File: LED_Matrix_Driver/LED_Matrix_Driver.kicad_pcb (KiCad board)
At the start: 4 copper layers, 200.7 x 66 mm, 73 parts, among them J1 Screw_Terminal_01x02, J2 LED Anode Rows, J3 Columns 24-31 LED Cathodes, J4 Columns 16-23 LED Cathodes, J5 Columns 8-15 LED Cathodes, J6 Columns 0-7 LED Cathodes, J7 Buttons, U1 ESP32-DEVKITC-32E, U2 74HCT244, U3 MIC2981, U4 74HC238, U5 HEF4794B, U6 HEF4794B, U7 HEF4794B, U8 HEF4794B

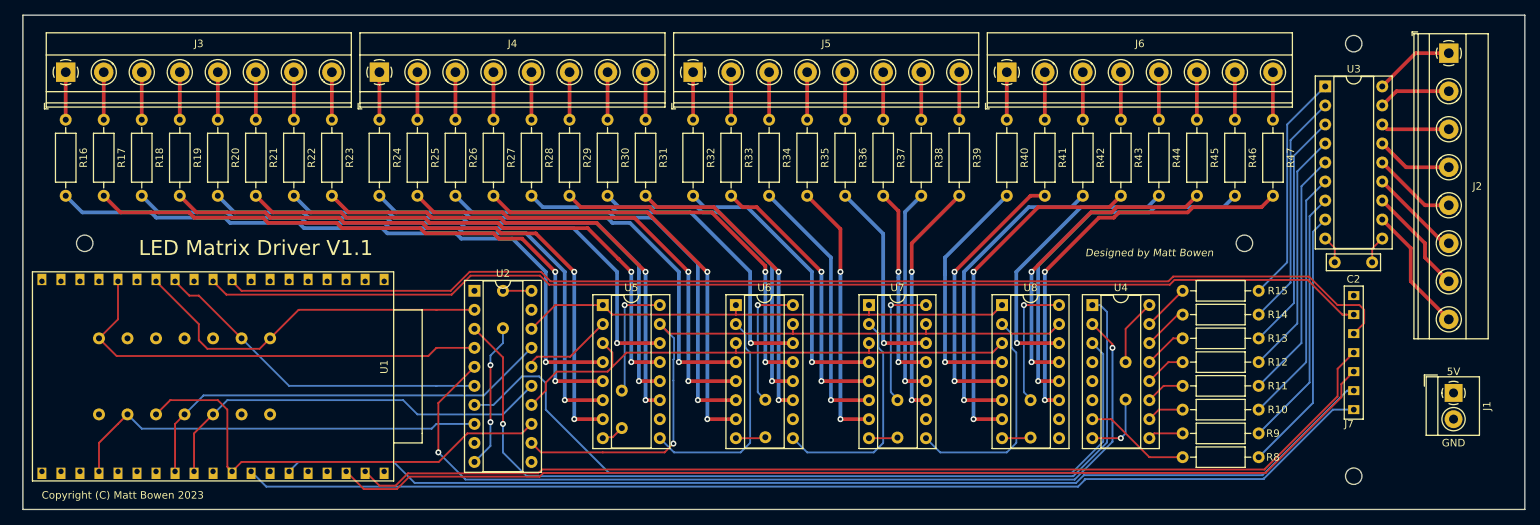
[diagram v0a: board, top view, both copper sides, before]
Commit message: Added audio input circuitry for potential audio applications
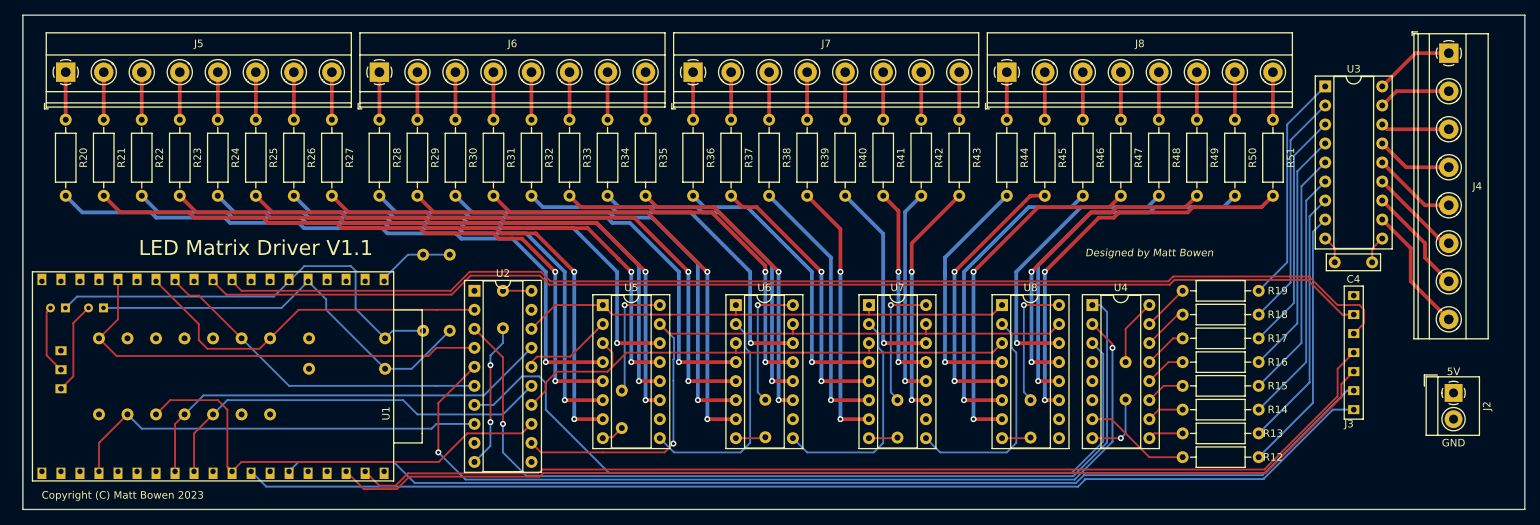
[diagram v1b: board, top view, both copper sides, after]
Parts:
- removed  : , MountingHole:MountingHole_2.2mm_M2 (x4)
- added C1: 1uF, Capacitor_THT:CP_Radial_D4.0mm_P2.00mm, B.Cu at (20.3, 49.3)
- added C2: 1uF, Capacitor_THT:CP_Radial_D4.0mm_P2.00mm, B.Cu at (15.2, 49.3)
- added J1: Audio In, Arduino:Custom_Pin_Header_3, B.Cu at (15.2, 62.0)
- added R1: 10k, Resistor_THT:R_Axial_DIN0207_L6.3mm_D2.5mm_P10.16mm_Horizontal, B.Cu at (66.5, 52.3)
- added R2: 10k, Resistor_THT:R_Axial_DIN0207_L6.3mm_D2.5mm_P10.16mm_Horizontal, B.Cu at (47.8, 57.4)
- added R3: 10k, Resistor_THT:R_Axial_DIN0207_L6.3mm_D2.5mm_P10.16mm_Horizontal, B.Cu at (63.0, 52.3)
- added R4: 10k, Resistor_THT:R_Axial_DIN0207_L6.3mm_D2.5mm_P10.16mm_Horizontal, B.Cu at (47.8, 53.3)
- J3: renamed from J7; footprint Arduino:Custom_Pin_Header -> Arduino:Custom_Pin_Header_7
- renumbered C1 to C3, C2 to C4, C3 to C5, C4 to C6, C5 to C7, C6 to C8, C7 to C9, J1 to J2, J2 to J4, J3 to J5, J4 to J6, J5 to J7, J6 to J8, R6 to R10, R7 to R11, R8 to R12, R9 to R13, R10 to R14, R11 to R15, R12 to R16, R13 to R17, R14 to R18, R15 to R19, R16 to R20, R17 to R21, R18 to R22, R19 to R23, R20 to R24, R21 to R25, R22 to R26, R23 to R27, R24 to R28, R25 to R29, R26 to R30, R27 to R31, R28 to R32, R29 to R33, R30 to R34, R31 to R35, R32 to R36, R33 to R37, R34 to R38, R35 to R39, R36 to R40, R37 to R41, R38 to R42, R39 to R43, R40 to R44, R41 to R45, R42 to R46, R43 to R47, R44 to R48, R45 to R49, R1 to R5, R46 to R50, R47 to R51, R2 to R6, R3 to R7, R4 to R8, R5 to R9
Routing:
- net Net-(C2-Pad1): track 0.00 -> 57.5 mm
- net Net-(C1-Pad1): track 0.00 -> 55.5 mm
- net Net-(C1-Pad2): track 0.00 -> 12.3 mm
- net Net-(R1-Pad2): track 0.00 -> 10.5 mm
- net Net-(C2-Pad2): track 0.00 -> 9.25 mm

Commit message: Created Gerber plots of new driver board design, button board, and new LED board As of 12/15/2023, all three PCBs have been submitted to JLCPCB for manufacturing.
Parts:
- added REF**: MountingHole_2.2mm_M2, MountingHole:MountingHole_2.2mm_M2, F.Cu at (173.4, 40.6)
- added REF**: MountingHole_2.2mm_M2, MountingHole:MountingHole_2.2mm_M2, F.Cu at (17.8, 40.6)
- added REF**: MountingHole_2.2mm_M2, MountingHole:MountingHole_2.2mm_M2, F.Cu at (187.3, 69.2)
- added REF**: MountingHole_2.2mm_M2, MountingHole:MountingHole_2.2mm_M2, F.Cu at (187.3, 14.0)
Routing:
- net Earth: vias 3 -> 11
- added copper zone on B.Cu, net Earth
- added copper zone on F.Cu, net Earth
